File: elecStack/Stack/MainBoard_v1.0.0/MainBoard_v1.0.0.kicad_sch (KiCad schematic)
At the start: 26 parts, among them J1 Conn_01x04_Socket, J2 Conn_01x06_Pin, J3 Conn_01x06_Pin, Q1 NMOS, Q2 NMOS, Q3 NMOS, Q4 NMOS, Q5 NMOS, Q6 NMOS, Q7 NMOS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

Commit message: IMU_connected
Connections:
- net RXD_2 is gone; now on net CS: U1.GP5
- net 3V3: now also J2.6 (Pin_6)
- net GND: now also J2.4 (Pin_4)
- net INT: now reaches U1.GP10
- net INT: now also J2.1 (Pin_1)
- net SCL: now reaches U1.GP11
- net SCL: now also J2.3 (Pin_3)
- net SDA: now reaches U1.GP12
- net SDA: now also J2.2 (Pin_2)
- net P0: now reaches U1.GP6
- net P0: now also J3.2 (Pin_2)
- net DI: now reaches U1.GP7
- net DI: now also J3.5 (Pin_5)
- net RST: now reaches U1.GP8
- net RST: now also J3.4 (Pin_4)
- net P1: now reaches U1.GP9
- net P1: now also J3.3 (Pin_3)
- net Bootloader: now reaches J3.1 (Pin_1)
- net CS: now reaches J3.6 (Pin_6)
- net 3V: now reaches J2.5 (Pin_5)
- net TXD_2: no longer names the net of U1.GP4
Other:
- note removed: "Make IMU connections over I2C"
- moved on the sheet: J2, J3

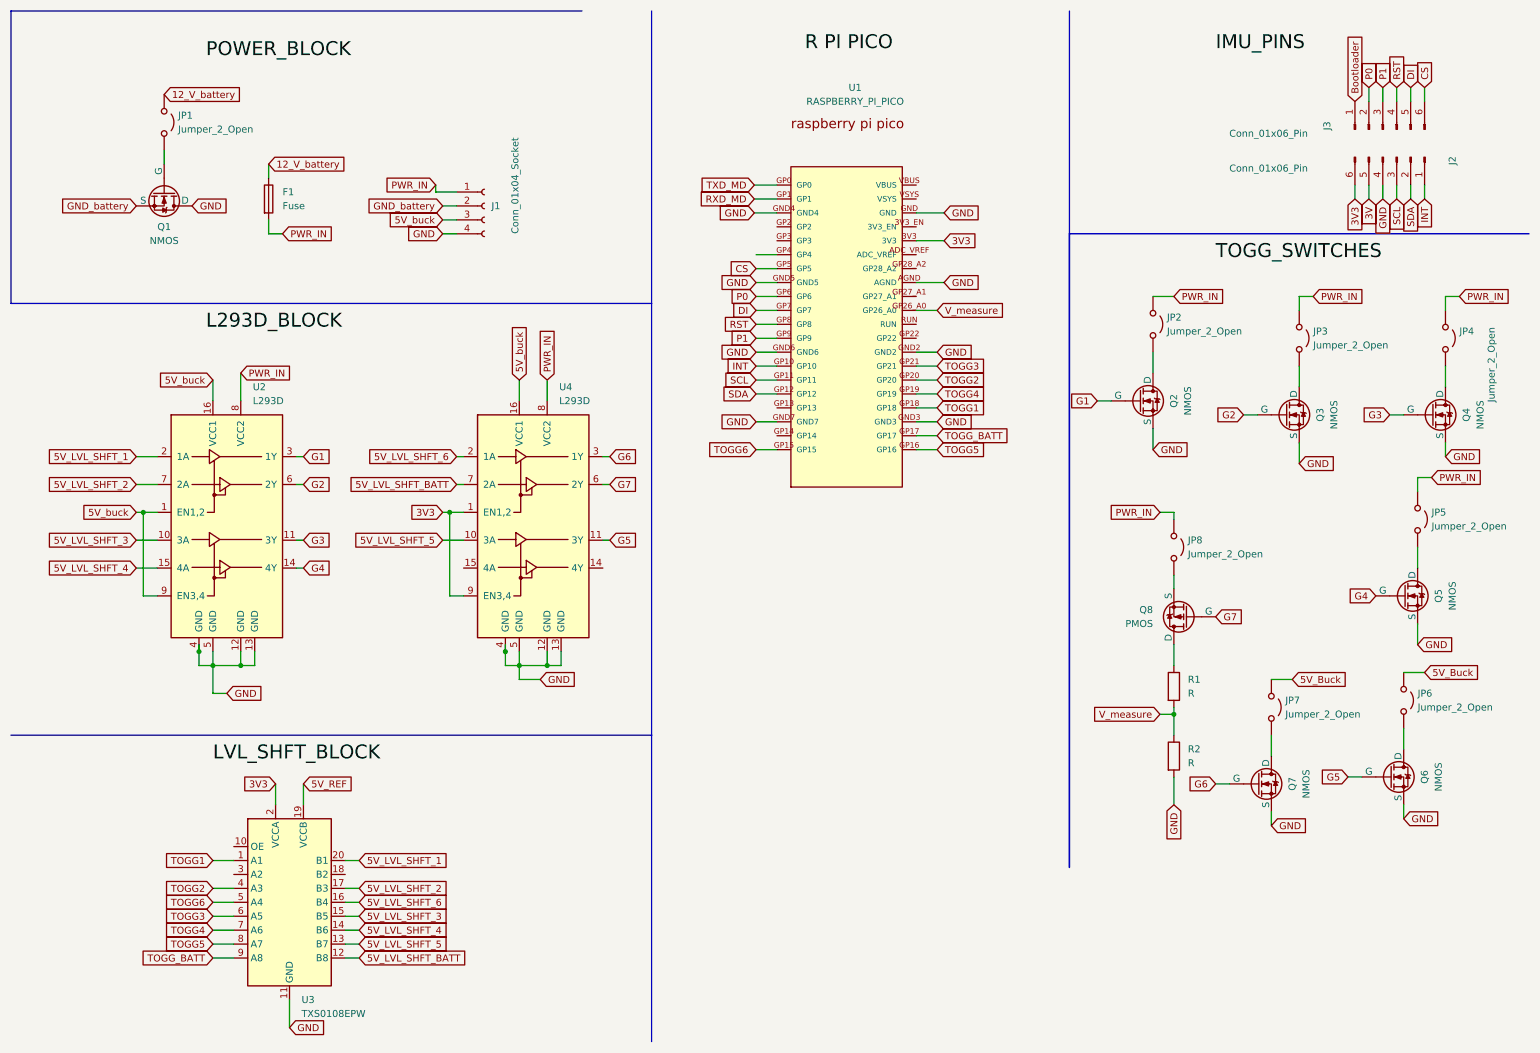
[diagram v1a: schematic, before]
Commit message: updated placements
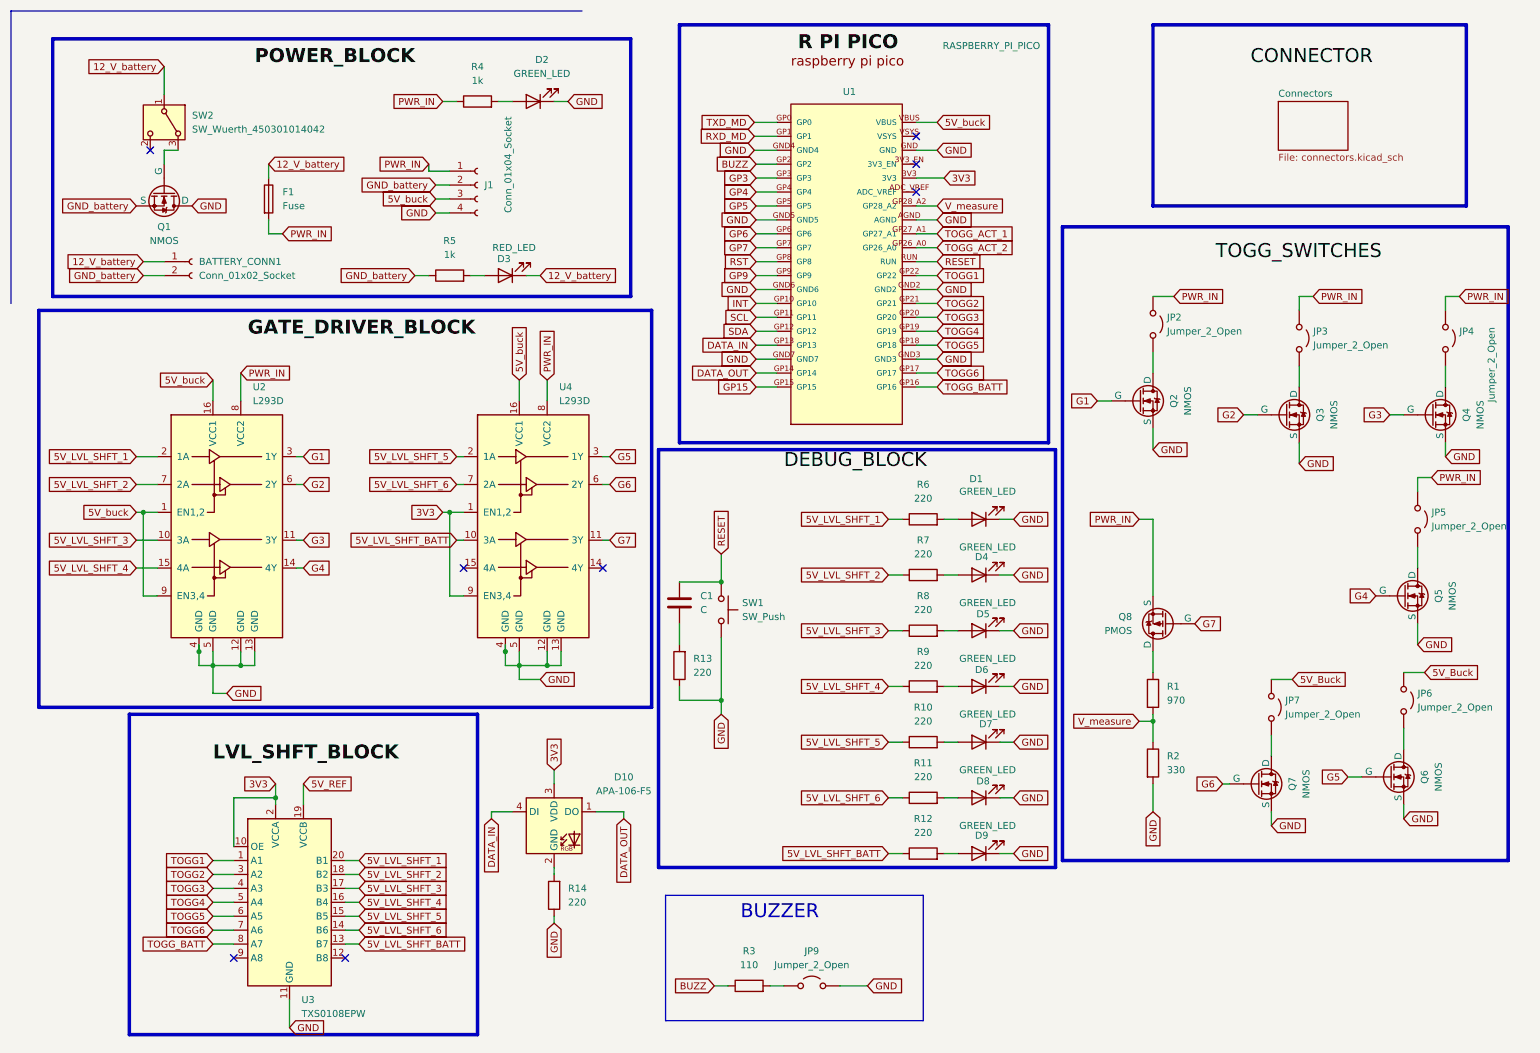
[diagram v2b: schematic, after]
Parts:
- removed J2, J3: Conn_01x06_Pin, symbol Connector:Conn_01x06_Pin
- removed JP1, JP8: Jumper_2_Open, symbol Jumper:Jumper_2_Open
- added BATTERY_CONN1: Conn_01x02_Socket, Connector_Phoenix_MSTB:PhoenixContact_MSTBA_2,5_2-G-5,08_1x02_P5.08mm_Horizontal, symbol Connector:Conn_01x02_Socket
- added C1: C, Capacitor_SMD:C_1210_3225Metric_Pad1.33x2.70mm_HandSolder, symbol Device:C
- added D1, D2, D4, D5, D6, D7, D8, D9: GREEN_LED, LED_SMD:LED_0805_2012Metric_Pad1.15x1.40mm_HandSolder, symbol Device:LED
- added D10: APA-106-F5, LED_THT:LED_D5.0mm-4_RGB, symbol LED:APA-106-F5
- added D3: RED_LED, LED_SMD:LED_0805_2012Metric_Pad1.15x1.40mm_HandSolder, symbol Device:LED
- added JP9: Jumper_2_Open, Connector_Phoenix_MSTB:PhoenixContact_MSTBA_2,5_2-G_1x02_P5.00mm_Horizontal, symbol Jumper:Jumper_2_Open
- added R10, R11, R12, R13, R14, R6, R7, R8, R9: 220, Resistor_SMD:R_0805_2012Metric_Pad1.20x1.40mm_HandSolder, symbol Device:R
- added R3: 110, Resistor_SMD:R_0805_2012Metric_Pad1.20x1.40mm_HandSolder, symbol Device:R
- added R4, R5: 1k, Resistor_SMD:R_0805_2012Metric_Pad1.20x1.40mm_HandSolder, symbol Device:R
- added SW1: SW_Push, Button_Switch_THT:SW_PUSH_6mm_H5mm, symbol Switch:SW_Push
- added SW2: SW_Wuerth_450301014042, Button_Switch_THT:SW_Slide-03_Wuerth-WS-SLTV_10x2.5x6.4_P2.54mm, symbol Switch:SW_Wuerth_450301014042
- F1: footprint (none) -> Fuse:Fuse_Blade_Mini_directSolder
- J1: footprint (none) -> Connector_Phoenix_MSTB:PhoenixContact_MSTBA_2,5_4-G_1x04_P5.00mm_Horizontal
- JP2, JP3, JP4, JP5, JP6, JP7: footprint (none) -> Connector_Phoenix_MSTB:PhoenixContact_MSTBA_2,5_2-G_1x02_P5.00mm_Horizontal
- Q1: footprint (none) -> Connector_Molex:IRF540N
- Q2, Q3, Q4, Q5, Q6, Q7, Q8: footprint (none) -> Connector_Molex:Molex_SPOX_5267-03A_1x03_P2.50mm_Vertical
- R1: value R -> 970; footprint (none) -> Resistor_SMD:R_0805_2012Metric_Pad1.20x1.40mm_HandSolder
- R2: value R -> 330; footprint (none) -> Resistor_SMD:R_0805_2012Metric_Pad1.20x1.40mm_HandSolder
- U1: footprint RASPBERRY_PI_PICO:RASPBERRY_PI_PICO -> RASPBERRY_PI_PICO.kicad_mod:RASPBERRY_PI_PICO
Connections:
- net 12_V_battery: now also BATTERY_CONN1.1 (Pin_1), D3.1 (K), SW2.1 (B)
- net 3V3: now also U3.10 (OE), D10.3 (VDD)
- net 5V_LVL_SHFT_1: now also R6.1
- net 5V_LVL_SHFT_2: now also U3.18 (B2), R7.1; no longer U3.17 (B3)
- net 5V_LVL_SHFT_3: now also U3.17 (B3), R8.1; no longer U3.15 (B5)
- net 5V_LVL_SHFT_4: now also U3.16 (B4), R9.1; no longer U3.14 (B6)
- net 5V_LVL_SHFT_5: now also U3.15 (B5), U4.2 (1A), R10.1; no longer U3.13 (B7), U4.10 (3A)
- net 5V_LVL_SHFT_6: now also U3.14 (B6), U4.7 (2A), R11.1; no longer U3.16 (B4), U4.2 (1A)
- net 5V_LVL_SHFT_BATT: now also U3.13 (B7), U4.10 (3A), R12.1; no longer U3.12 (B8), U4.7 (2A)
- net 5V_buck: now also U1.VBUS
- net G5: now also U4.3 (1Y); no longer U4.11 (3Y)
- net G6: now also U4.6 (2Y); no longer U4.3 (1Y)
- net G7: now also U4.11 (3Y); no longer U4.6 (2Y)
- net GND: now also D1.1 (K), D2.1 (K), D4.1 (K), D5.1 (K), D6.1 (K), D7.1 (K), D8.1 (K), D9.1 (K), JP9.2 (B), R13.1, R14.1, SW1.2
- net GND_battery: now also BATTERY_CONN1.2 (Pin_2), R5.1
- net PWR_IN: now also Q8.3 (S), R4.1
- net TOGG1: now also U1.GP22; no longer U1.GP18
- net TOGG2: now also U1.GP21, U3.3 (A2); no longer U1.GP20, U3.4 (A3)
- net TOGG3: now also U1.GP20, U3.4 (A3); no longer U1.GP21, U3.6 (A5)
- net TOGG4: now also U3.5 (A4); no longer U3.7 (A6)
- net TOGG5: now also U1.GP18, U3.6 (A5); no longer U1.GP16, U3.8 (A7)
- net TOGG6: now also U1.GP17, U3.7 (A6); no longer U1.GP15, U3.5 (A4)
- net TOGG_BATT: now also U1.GP16, U3.8 (A7); no longer U1.GP17, U3.9 (A8)
- net V_measure: now also U1.GP28_A2; no longer U1.GP26_A0
- net at Q1.2 (G): now also SW2.3 (A)
- net DATA_IN: now reaches U1.GP13
- net DATA_IN: now also D10.4 (DI)
- net DATA_OUT: now reaches U1.GP14
- net DATA_OUT: now also D10.1 (DO)
- net BUZZ: now reaches U1.GP2
- net BUZZ: now also R3.1
- net TOGG_ACT_1: now reaches U1.GP27_A1
- net GP3: now reaches U1.GP3
- net GP4: now reaches U1.GP4
- net RESET: now reaches U1.RUN
- net RESET: now also C1.2, SW1.1
- net CS renamed GP5
- net DI renamed GP7
- net P0 renamed GP6
- net P1 renamed GP9
- new net: D8.2 (A), R11.2
- new net: D2.2 (A), R4.2
- new net: JP9.1 (A), R3.2
- new net: D4.2 (A), R7.2
- new net: D7.2 (A), R10.2
- new net: D1.2 (A), R6.2
- new net: D6.2 (A), R9.2
- new net: D10.2 (GND), R14.2
- new net: D3.2 (A), R5.2
- new net: C1.1, R13.2
- new net: D9.2 (A), R12.2
- new net: D5.2 (A), R8.2
- new net GP15: U1.GP15
- new net TOGG_ACT_2: U1.GP26_A0
- no-connect marks 0 -> 8
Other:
- added sheet Connectors (connectors.kicad_sch)
- note added: "BUZZER"
- moved on the sheet: J1, Q8, R1, R2, U1
